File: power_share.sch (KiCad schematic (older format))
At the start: 14 parts, among them J1 Conn_01x02, J2 Conn_01x03, Q1 IRLR8726PBF, Q2 IRLR8726PBF, U1 LTC4370

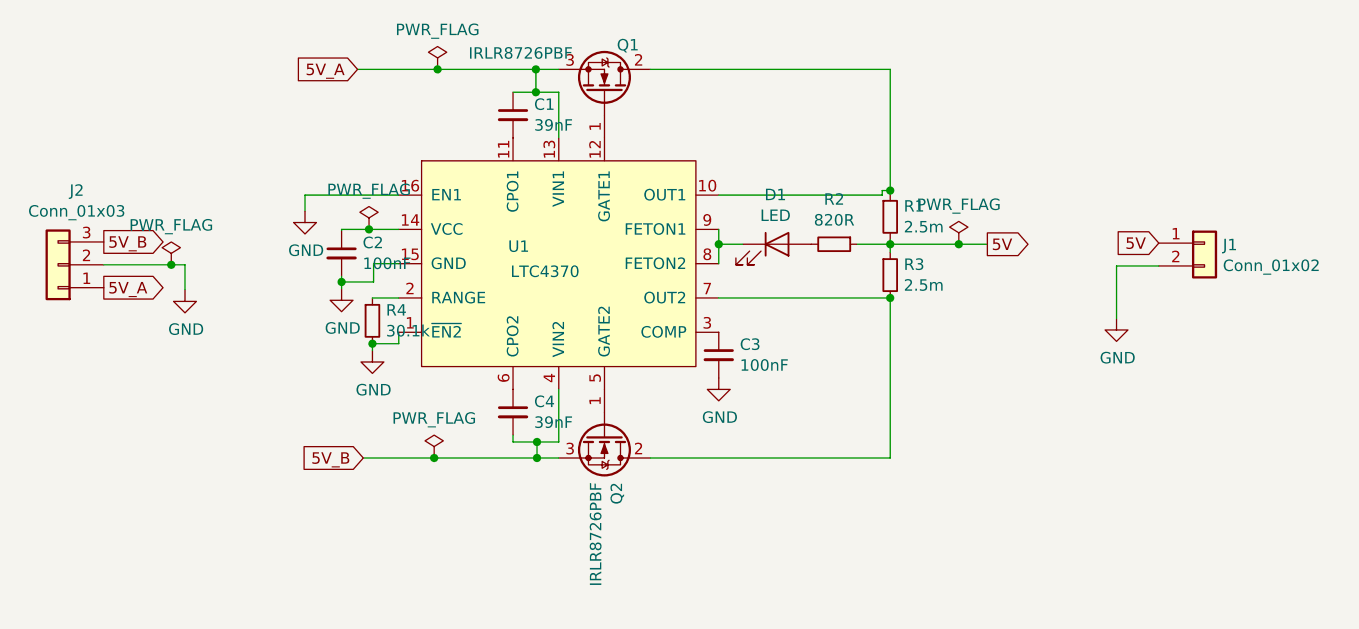
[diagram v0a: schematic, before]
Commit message: Redesigned layout
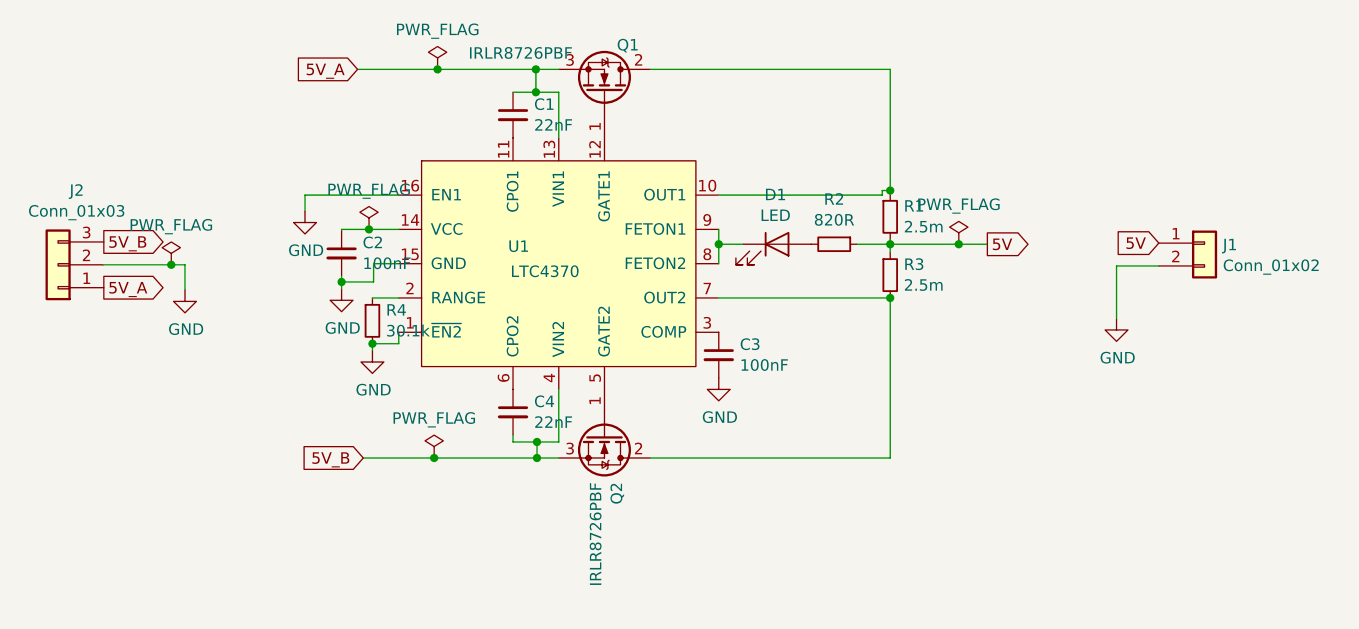
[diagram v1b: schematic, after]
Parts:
- C1, C4: value 39nF -> 22nF; footprint Capacitor_SMD:C_0603_1608Metric_Pad1.05x0.95mm_HandSolder -> Capacitor_SMD:C_0402_1005Metric
- C2, C3: footprint Capacitor_SMD:C_0603_1608Metric_Pad1.05x0.95mm_HandSolder -> Capacitor_SMD:C_0402_1005Metric
- Q1, Q2: footprint Package_TO_SOT_SMD:TO-252-3_TabPin4 -> Package_TO_SOT_SMD:TO-252-2
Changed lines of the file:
@@
 P 5370 4165
 F 0 "C4" H 5462 4211 50  0000 L CNN
-F 1 "39nF" H 5462 4120 50  0000 L CNN
-F 2 "Capacitor_SMD:C_0603_1608Metric_Pad1.05x0.95mm_HandSolder" H 5370 4165 50  0001 C CNN
+F 1 "22nF" H 5462 4120 50  0000 L CNN
+F 2 "Capacitor_SMD:C_0402_1005Metric" H 5370 4165 50  0001 C CNN
 F 3 "~" H 5370 4165 50  0001 C CNN
 	1    5370 4165
@@
 F 0 "C3" H 6362 3961 50  0000 L CNN
 F 1 "100nF" H 6362 3870 50  0000 L CNN
-F 2 "Capacitor_SMD:C_0603_1608Metric_Pad1.05x0.95mm_HandSolder" H 6270 3915 50  0001 C CNN
+F 2 "Capacitor_SMD:C_0402_1005Metric" H 6270 3915 50  0001 C CNN
 F 3 "~" H 6270 3915 50  0001 C CNN
 	1    6270 3915
@@
 P 5370 2865
 F 0 "C1" H 5462 2911 50  0000 L CNN
-F 1 "39nF" H 5462 2820 50  0000 L CNN
-F 2 "Capacitor_SMD:C_0603_1608Metric_Pad1.05x0.95mm_HandSolder" H 5370 2865 50  0001 C CNN
+F 1 "22nF" H 5462 2820 50  0000 L CNN
+F 2 "Capacitor_SMD:C_0402_1005Metric" H 5370 2865 50  0001 C CNN
 F 3 "~" H 5370 2865 50  0001 C CNN
 	1    5370 2865
@@
 F 0 "Q1" V 5976 2819 50  0000 L CNN
 F 1 "IRLR8726PBF" V 5940 2170 50  0000 L CNN
-F 2 "Package_TO_SOT_SMD:TO-252-3_TabPin4" H 5970 2665 50  0001 L CNN
+F 2 "Package_TO_SOT_SMD:TO-252-2" H 5970 2665 50  0001 L CNN
 F 3 "http://www.irf.com/product-info/datasheets/data/irf8721pbf-1.pdf" H 5670 2765 50  0001 L CNN
 	1    5770 2765
@@
 F 0 "Q2" H 5976 4319 50  0000 L CNN
 F 1 "IRLR8726PBF" H 5976 4228 50  0000 L CNN
-F 2 "Package_TO_SOT_SMD:TO-252-3_TabPin4" H 5970 4165 50  0001 L CNN
+F 2 "Package_TO_SOT_SMD:TO-252-2" H 5970 4165 50  0001 L CNN
 F 3 "http://www.irf.com/product-info/datasheets/data/irf8721pbf-1.pdf" H 5670 4265 50  0001 L CNN
 	1    5770 4265
@@
 F 0 "C2" H 4712 3516 50  0000 L CNN
 F 1 "100nF" H 4712 3425 50  0000 L CNN
-F 2 "Capacitor_SMD:C_0603_1608Metric_Pad1.05x0.95mm_HandSolder" H 4620 3470 50  0001 C CNN
+F 2 "Capacitor_SMD:C_0402_1005Metric" H 4620 3470 50  0001 C CNN
 F 3 "~" H 4620 3470 50  0001 C CNN
 	1    4620 3470
